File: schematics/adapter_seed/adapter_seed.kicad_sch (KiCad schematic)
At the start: 2 parts, among them J1 Conn_02x20_Odd_Even

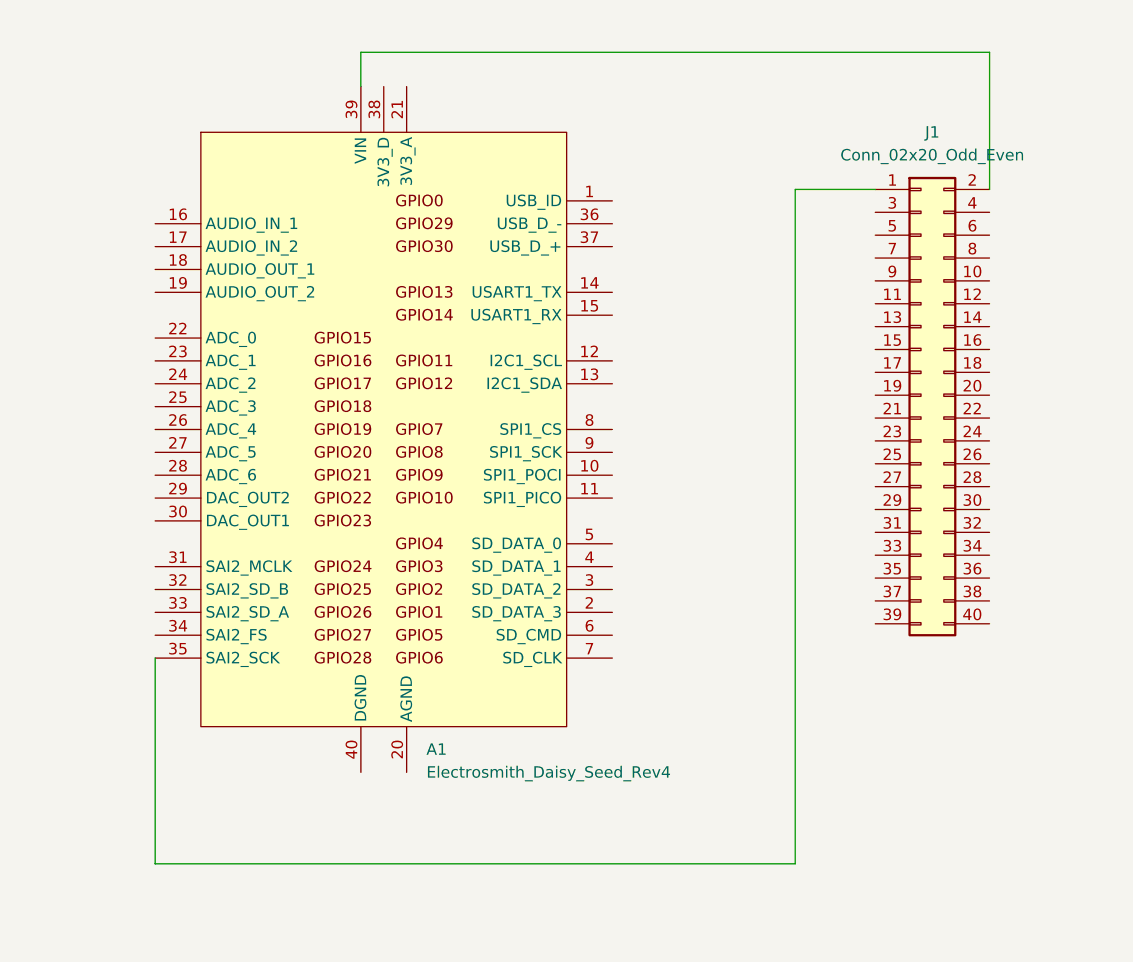
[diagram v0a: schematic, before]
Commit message: daisy seed adapter board: initial layout
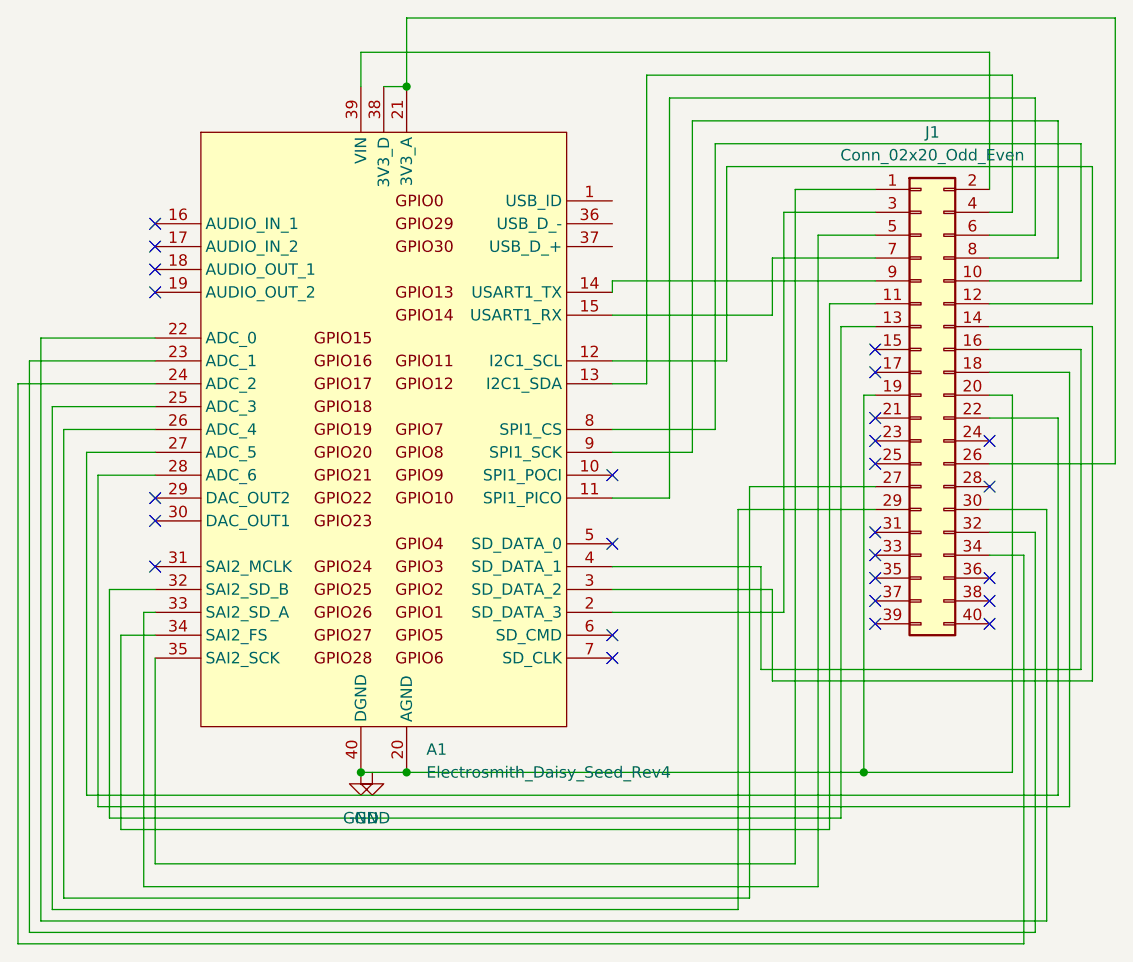
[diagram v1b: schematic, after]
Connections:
- net at J1.10 (Pin_10): now also A1.8 (SPI1_CS)
- net at J1.11 (Pin_11): now also A1.34 (SAI2_FS)
- net at J1.12 (Pin_12): now also A1.12 (I2C1_SCL)
- net at J1.13 (Pin_13): now also A1.32 (SAI2_SD_B)
- net at J1.14 (Pin_14): now also A1.3 (SD_DATA_2)
- net at J1.16 (Pin_16): now also A1.4 (SD_DATA_1)
- net at J1.18 (Pin_18): now also A1.28 (ADC_6)
- net GND: now reaches J1.19 (Pin_19)
- net GND: now also A1.20 (AGND), A1.40 (DGND), J1.20 (Pin_20)
- net at J1.22 (Pin_22): now also A1.27 (ADC_5)
- net at J1.26 (Pin_26): now also A1.21 (3V3_A), A1.38 (3V3_D)
- net at J1.27 (Pin_27): now also A1.26 (ADC_4)
- net at J1.29 (Pin_29): now also A1.25 (ADC_3)
- net at J1.3 (Pin_3): now also A1.2 (SD_DATA_3)
- net at J1.30 (Pin_30): now also A1.22 (ADC_0)
- net at J1.32 (Pin_32): now also A1.23 (ADC_1)
- net at J1.34 (Pin_34): now also A1.24 (ADC_2)
- net at J1.4 (Pin_4): now also A1.13 (I2C1_SDA)
- net at J1.5 (Pin_5): now also A1.33 (SAI2_SD_A)
- net at J1.6 (Pin_6): now also A1.11 (SPI1_PICO)
- net at J1.7 (Pin_7): now also A1.15 (USART1_RX)
- net at J1.8 (Pin_8): now also A1.9 (SPI1_SCK)
- net at J1.9 (Pin_9): now also A1.14 (USART1_TX)
- no-connect marks 0 -> 26

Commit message: pcb: minor corrections
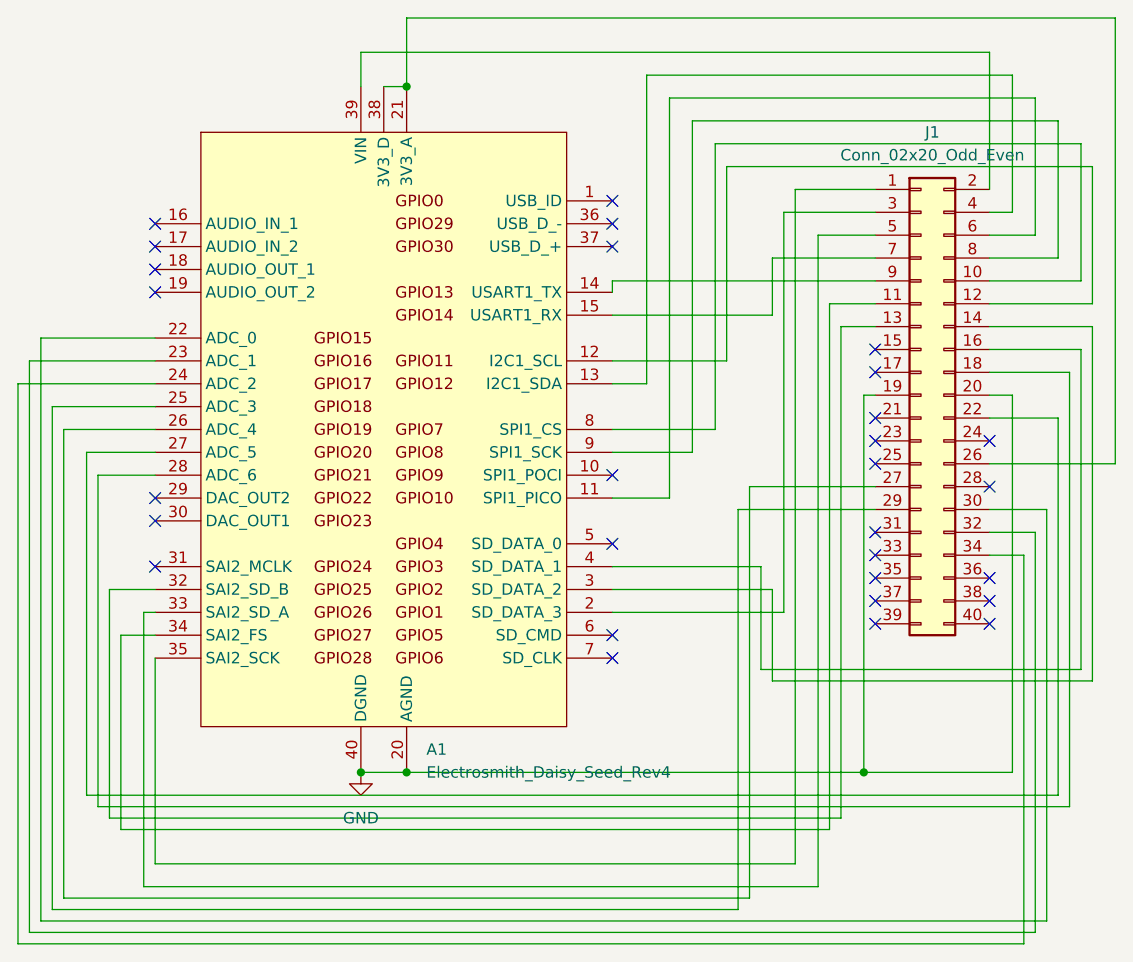
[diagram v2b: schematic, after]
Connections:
- no-connect marks 26 -> 29
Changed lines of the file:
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@@
   (no_connect (at 158.75 120.65))
   (no_connect (at 66.04 81.28))
+  (no_connect (at 116.84 78.74))
   (no_connect (at 158.75 105.41))
   (no_connect (at 66.04 88.9))
   (no_connect (at 158.75 125.73))
+  (no_connect (at 116.84 81.28))
   (no_connect (at 116.84 127))
   (no_connect (at 116.84 129.54))
   (no_connect (at 146.05 107.95))
   (no_connect (at 146.05 115.57))
+  (no_connect (at 116.84 83.82))
   (no_connect (at 146.05 120.65))
   (no_connect (at 146.05 118.11))
@@
     (stroke (width 0) (type default))
   )
+  (wire (pts (xy 161.29 100.33) (xy 158.75 100.33))
+    (stroke (width 0) (type default))
+  )
+  (wire (pts (xy 50.8 99.06) (xy 66.04 99.06))
+    (stroke (width 0) (type default))
+  )
+  (wire (pts (xy 134.62 132.08) (xy 134.62 121.92))
+    (stroke (width 0) (type default))
+  )
+  (wire (pts (xy 161.29 64.77) (xy 120.65 64.77))
+    (stroke (width 0) (type default))
+  )
   (wire (pts (xy 88.9 142.24) (xy 93.98 142.24))
-    (stroke (width 0) (type default))
-  )
-  (wire (pts (xy 161.29 100.33) (xy 158.75 100.33))
-    (stroke (width 0) (type default))
-  )
-  (wire (pts (xy 50.8 99.06) (xy 66.04 99.06))
-    (stroke (width 0) (type default))
-  )
-  (wire (pts (xy 134.62 132.08) (xy 134.62 121.92))
-    (stroke (width 0) (type default))
-  )
-  (wire (pts (xy 161.29 64.77) (xy 120.65 64.77))
     (stroke (width 0) (type default))
   )
@@
         )
       )
-    )
-  )
-  (symbol (lib_id "power:GND") (at 90.17 142.24 0) (unit 1)
-    (in_bom yes) (on_board yes) (dnp no) (fields_autoplaced)
-    (property "Reference" "#PWR02" (at 90.17 148.59 0)
-      (effects (font (size 1.27 1.27)) hide)
-    )
-    (property "Value" "GND" (at 90.17 147.32 0)
-      (effects (font (size 1.27 1.27)))
-    )
-    (property "Footprint" "" (at 90.17 142.24 0)
-      (effects (font (size 1.27 1.27)) hide)
-    )
-    (property "Datasheet" "" (at 90.17 142.24 0)
-      (effects (font (size 1.27 1.27)) hide)
-    )
-    (pin "1")
-    (instances
-      (project "adapter_seed"
-        (path "/dcc40942-4d11-4052-9d31-5225207a5e0a"
-          (reference "#PWR02") (unit 1)
-        )
-      )
